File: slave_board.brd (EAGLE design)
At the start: 200 x 100 mm, 163 parts, among them IC3 ATMEGA2560-16AU, J1 OSTVN08A150, J11 1935161, J12 OSTVN06A150, J13 OSTVN08A150, J17 RJ45, J18 OSTVN08A150, J2 OSTVN08A150, J22 RJ45, J3 1935161, J4 OSTVN06A150, J6 1935161, J8 OSTVN08A150, K1 ORWH-SH-112D1F, Q1 PHB45NQ15T, Q2 PHB45NQ15T, Q3 BSS138L, Q5 BSS138L, Q7 PHB45NQ15T, Q8 IRFR9024TRPBF, U1 VNQ5E160KTR-E, U2 PCA9615, U3 INA213AIDCKT, U4 VNH7070ASTR, U5 VNH7070ASTR, U6 VNQ5E160KTR-E, U7 INA213AIDCKT, U8 LM340MP-5.0/NOPB, U9 LM340MP-5.0/NOPB, Y1 ABLS-16.000MHZ-B4-T

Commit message: Morning changes from board review
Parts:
- removed J12: OSTVN06A150, smoothio:6PIN_SCREW_TERMINAL
- added J16: OSTVN08A150, smoothio:8PIN_SCREW_TERMINAL
- added L1: 742792651, smoothio:742792651
- added R27, R28, R29, R30: 10k, SparkFun-Resistors:0603
- J1, J2: value OSTVN08A150 -> OSTVN06A150; device smoothio:8PIN_SCREW_TERMINAL -> smoothio:6PIN_SCREW_TERMINAL
- J5: value (none) -> OSTVN06A150; device SparkFun-Connectors:1X05 -> smoothio:6PIN_SCREW_TERMINAL
- moved J14 26.3 mm to (66.5, 29.1), turned to 0 degrees
- moved J5 14.5 mm to (84.7, 99.4), turned to 180 degrees
- moved J2 6.54 mm to (111.0, 99.4), turned to 180 degrees
- moved J1 6.50 mm to (139.9, 92.9)
- moved C18 1.59 mm to (96.4, 81.6)
- moved C30 1.59 mm to (103.0, 89.7)
- moved C15 1.59 mm to (96.7, 81.2)
- moved C31 1.59 mm to (92.9, 81.6)
- moved D6 1.59 mm to (100.5, 75.5)
- moved TP2 1.59 mm to (104.0, 72.3)
- moved JP19 1.59 mm to (96.7, 88.1)
- moved TP19 1.59 mm to (95.9, 90.7)
- moved U9 1.59 mm to (103.5, 83.1)
- moved J4 0.37 mm to (156.5, 93.0)
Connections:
- removed net CUP_SENSE0: IC3.72, J4.5
- removed net CUP_SENSE1: IC3.71, J12.5
- new net GND2: C19.-, C20.-, C21.-, D3.1, D3.3, D5.1, D5.3, L1.P$1, R1.1, R14.1, U3.5, U7.5
- new net LIMIT_SENSE: IC3.70, J1.1, R28.2
- net +5V: now also J1.3, J1.6, J16.5, J16.8, R27.1, R28.1, R29.1, R30.1; no longer J1.8, J12.3, J12.6, J2.5
- net A1: now also J5.3; no longer J5.2
- net A2: now also J5.2; no longer J5.1
- net B1: now also J5.4; no longer J5.3
- net B2: now also J5.5; no longer J5.4
- net CAROUSEL_POS: now also J1.4, R27.2; no longer J1.6
- net CUP_MASS1: now also J4.5; no longer J12.2
- net ELEV_ENC_A: now also J16.6, R29.2; no longer J2.8
- net ELEV_ENC_B: now also J16.3, R30.2; no longer J2.7
- net GND: now also J1.2, J16.1, J16.4, J16.7, L1.P$2; no longer C19.-, C20.-, C21.-, D3.1, D3.3, D5.1, D5.3, J1.1, J1.3, J1.7, J12.1, J12.4, R1.1, R14.1, U3.5, U7.5
- net THERMISTOR0: now also J2.5; no longer J1.2
- net THERMISTOR1: now also J16.2; no longer J1.4
- net V-STEPPER: now also J5.6; no longer J5.5
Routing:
- net GND: track 438.9 -> 341.9 mm, vias 62 -> 60
- net CUP_SENSE1: track 59.8 -> 0.00 mm, vias 1 -> 0
- net GND2: track 0.00 -> 54.9 mm, vias 0 -> 2
- net CUP_SENSE0: track 42.9 -> 0.00 mm, vias 1 -> 0
- net BLENDER0_EN: track 130.9 -> 104.1 mm, vias 3 -> 2
- net PIVOT_ENC_A: track 31.1 -> 4.73 mm
- net STEP: track 59.2 -> 33.0 mm
- net DIR: track 57.3 -> 32.6 mm
- net V-STEPPER: track 30.6 -> 8.13 mm
- net CAROUSEL_POS: track 40.9 -> 21.4 mm
- net THERMISTOR1: track 40.0 -> 21.0 mm
- net CUP_MASS1: track 62.7 -> 45.5 mm
- net CUP_MASS0: track 46.6 -> 31.0 mm
- net +5V: track 415.4 -> 401.0 mm
- net BLENDER1_EN: track 131.5 -> 117.7 mm, vias 4 -> 3
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
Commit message: Finished review changes
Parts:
- removed R27: 10k, SparkFun-Resistors:0603
- moved R28 187.8 mm to (156.4, 90.3), turned to 180 degrees
- moved R29 181.1 mm to (145.8, 90.6)
- moved R30 179.1 mm to (140.9, 90.6), turned to 180 degrees
- moved L1 99.9 mm to (55.9, 60.4), flipped to the bottom
- moved DRV8825 22.8 mm to (69.2, 75.1), turned to 0 degrees
- moved TP16 21.7 mm to (64.7, 96.2)
- moved R23 19.4 mm to (117.1, 90.7), turned to 180 degrees
- moved C34 19.4 mm to (117.1, 88.2), turned to 180 degrees
- moved J4 17.5 mm to (174.0, 93.0)
- moved C29 15.6 mm to (164.0, 87.6)
- moved R19 15.6 mm to (164.0, 90.2)
- moved J1 14.1 mm to (154.0, 93.0)
- moved TP6 12.1 mm to (123.6, 96.0)
- moved C10 10.3 mm to (132.5, 88.0), turned to 0 degrees
- moved R3 10.2 mm to (132.5, 90.5), turned to 0 degrees
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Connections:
- net +5V: no longer R27.1
- net CAROUSEL_POS: no longer R27.2
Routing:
- net V-STEPPER: track 8.13 -> 48.5 mm
- net +5V: track 401.0 -> 440.3 mm, vias 10 -> 11
- net LIMIT_SENSE: track 0.00 -> 38.9 mm
- net CAROUSEL_POS: track 21.4 -> 58.6 mm
- net CUP_MASS0: track 31.0 -> 65.0 mm
- net PIVOT_ENC_A: track 4.73 -> 33.7 mm
- net GND: track 341.9 -> 368.8 mm, vias 60 -> 42
- net CUP_MASS1: track 45.5 -> 72.4 mm
- net STEP: track 33.0 -> 56.3 mm
- net /EN: track 50.9 -> 74.2 mm, vias 2 -> 1
- net M0: track 46.6 -> 69.7 mm, vias 1 -> 2
- net DIR: track 32.6 -> 51.7 mm, vias 2 -> 0
- net M1: track 48.4 -> 67.5 mm, vias 1 -> 2
- net ELEV_ENC_B: track 44.4 -> 57.3 mm
- net M2: track 53.0 -> 65.7 mm, vias 1 -> 2
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- added copper zone on layer 1, net GND2
- added copper zone on layer 16, net GND2
- removed copper zone on layer 1, net GND

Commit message: Few more changes
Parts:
- added J12: (no value), SparkFun-Connectors:1X02
- moved J14 25.7 mm to (70.2, 3.63), turned to 180 degrees
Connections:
- net BLENDER0_EN: now also J12.1; no longer J14.1
- net BLENDER0_GATE: now also J14.1
- net BLENDER1_EN: now also J12.2; no longer J14.2
- net BLENDER1_GATE: now also J14.2
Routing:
- net BLENDER0_GATE: track 22.2 -> 44.2 mm, vias 0 -> 2
- net BLENDER1_GATE: track 22.5 -> 32.3 mm
- net CURR_SENS0: track 131.5 -> 132.5 mm
- net GND: track 368.8 -> 368.3 mm

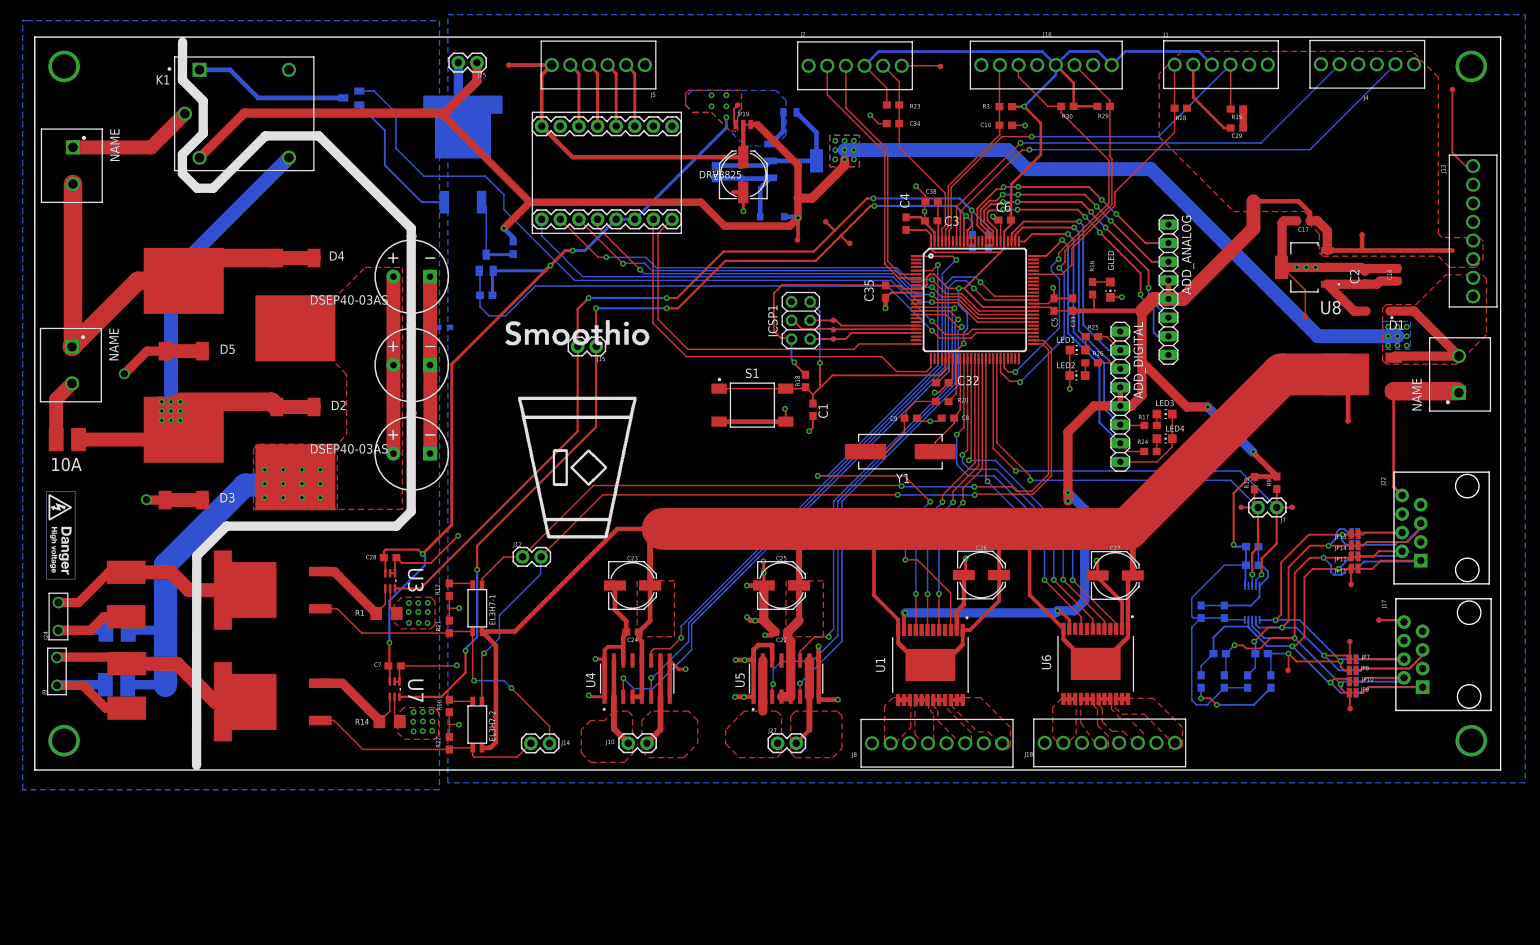
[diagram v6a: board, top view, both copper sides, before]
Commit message: Renumbered components
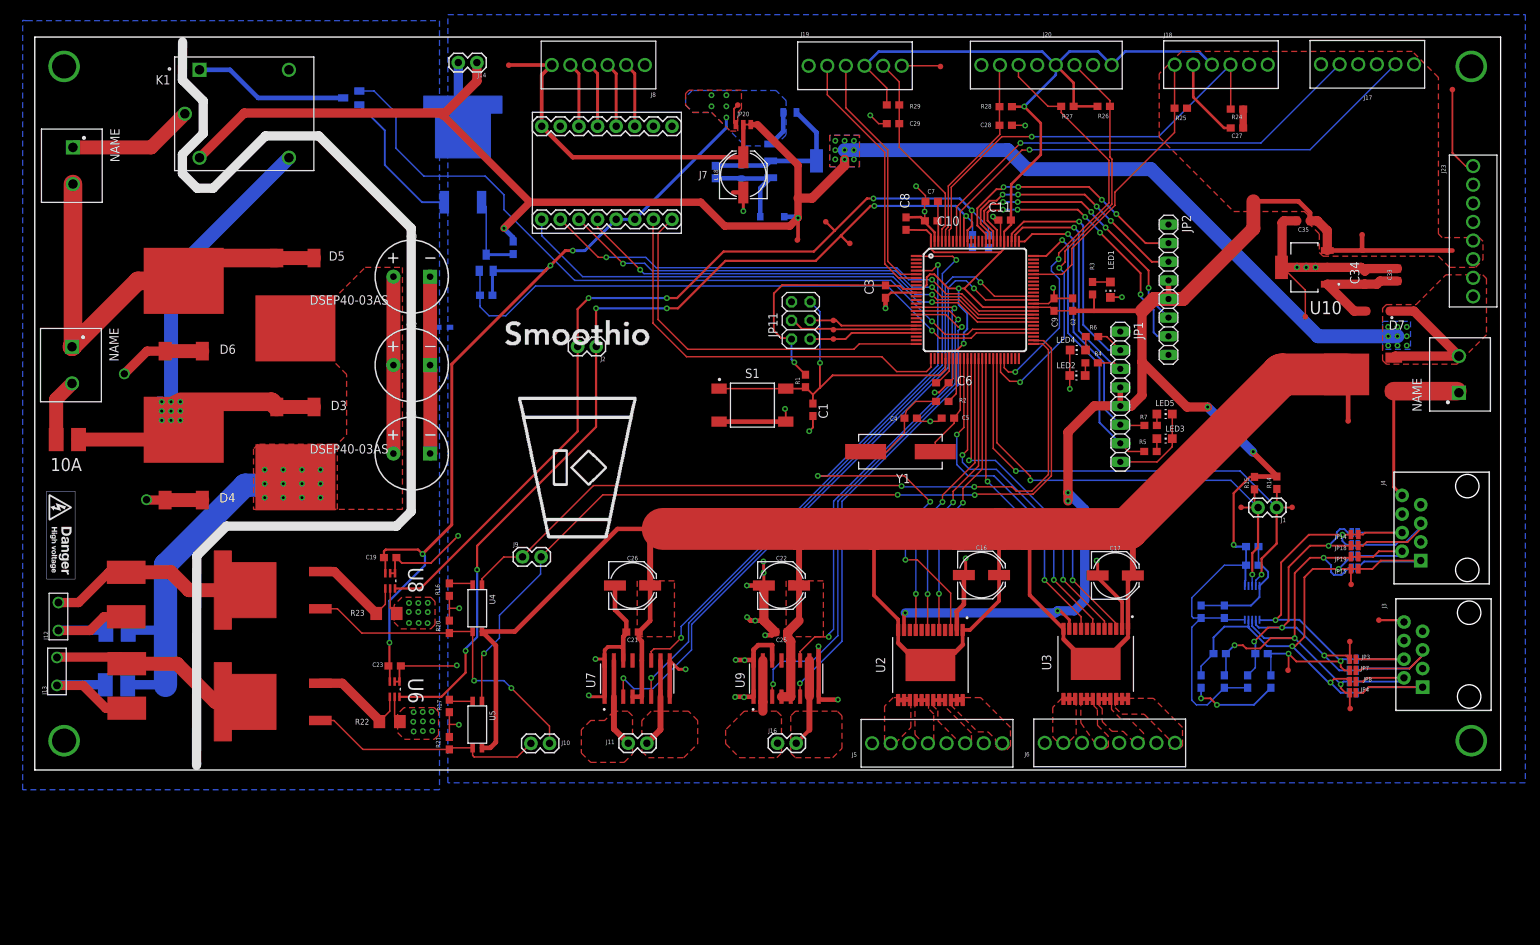
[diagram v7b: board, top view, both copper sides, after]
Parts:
- removed ADD_ANALOG: 8x1F-H8.5, SmartPrj:1X08
- removed DRV8825: DRV8825CARRIER, smoothio:DRV8825CARRIER
- removed EL3H7-1, EL3H7-2: EL3H7, smoothio:EL3H7
- removed GLED: GREEN, led:CHIP-LED0805
- removed ICSP1: 3x2M, SmartPrj:2X03
- removed J24: (no value), SparkFun-Connectors:1X02_BIG
- removed J25, J27: (no value), SparkFun-Connectors:1X02
- removed Q7: PHB45NQ15T, smoothio:PHB45NQ15T
- added J19: OSTVN06A150, smoothio:6PIN_SCREW_TERMINAL
- added J20, J23: OSTVN08A150, smoothio:8PIN_SCREW_TERMINAL
- added J21: 1935161, 1935161:PHOENIX_1935161
- added JP20: JUMPER-SMT_3_1-NC_TRACE_NO-SILK, SparkFun-Jumpers:SMT-JUMPER_3_1-NC_TRACE_NO-SILK
- added JP6: JUMPER-SMT_2_NO_NO-SILK, SparkFun-Jumpers:SMT-JUMPER_2_NO_NO-SILK
- added LED5: GREEN, led:CHIP-LED0805
- added Q4: PHB45NQ15T, smoothio:PHB45NQ15T
- added U10, U11: LM340MP-5.0/NOPB, LM340MP-5.0_NOPB:SOT230P700X180-4N
- C10: value 0.1uF -> 100n; device SparkFun-Capacitors:0603 -> rcl:C0603
- C11: value 0.1uF -> 100n
- C14: value 1.0uF -> 0.1uF
- C15: value 47uF -> 1.0uF; device SparkFun-Capacitors:PANASONIC_D -> rcl:C0603
- C16: value 1.0uF -> 47uF; device SparkFun-Capacitors:0603 -> SparkFun-Capacitors:PANASONIC_D
- C17: value 10uF -> 47uF; device SparkFun-Capacitors:0805 -> SparkFun-Capacitors:PANASONIC_D
- C18: value 100n -> 47uF; device SmartPrj:C0603-ROUND -> SparkFun-Capacitors:PANASONIC_D
- C19, C20, C21: value UCS2E470MHD1TO -> 0.1uF; device smoothio:UCS2E470MHD1TO -> rcl:C0603
- C2: value 100n -> 4.7uF; device SmartPrj:C0603-ROUND -> rcl:C0603
- C22: value 0.1uF -> 47uF; device rcl:C0603 -> SparkFun-Capacitors:PANASONIC_D
- C23, C25: value 47uF -> 0.1uF; device SparkFun-Capacitors:PANASONIC_D -> rcl:C0603
- C27: value 47uF -> 0.1uF; device SparkFun-Capacitors:PANASONIC_D -> SparkFun-Capacitors:0603
- C28: device rcl:C0603 -> SparkFun-Capacitors:0603
- C30: value 10uF -> UCS2E470MHD1TO; device SparkFun-Capacitors:0805 -> smoothio:UCS2E470MHD1TO
- C31: value 1.0uF -> UCS2E470MHD1TO; device SparkFun-Capacitors:0603 -> smoothio:UCS2E470MHD1TO
- C32: value 100n -> UCS2E470MHD1TO; device rcl:C0603 -> smoothio:UCS2E470MHD1TO
- C33: value 4.7uF -> 1.0uF; device rcl:C0603 -> SparkFun-Capacitors:0603
- C34: value 0.1uF -> 100n; device SparkFun-Capacitors:0603 -> SmartPrj:C0603-ROUND
- C35: value 100n -> 10uF; device rcl:C0603 -> SparkFun-Capacitors:0805
- C36, C7: value 0.1uF -> 1.0uF; device rcl:C0603 -> SparkFun-Capacitors:0603
- C37: value 0.1uF -> 100n; device rcl:C0603 -> SmartPrj:C0603-ROUND
- C38: value 1.0uF -> 10uF; device SparkFun-Capacitors:0603 -> SparkFun-Capacitors:0805
- C4: value 100n -> 15pF
- C5: value 100nF -> 15pF
- C8: value 15pF -> 100n
- C9: value 15pF -> 100nF
- D1: value MBR0530 -> SK520TR; device smoothio:MBR0530 -> smoothio:SK520TR
- D2: value DSEP40-03AS -> SK520TR; device smoothio:DSEP40-03AS -> smoothio:SK520TR
- D6: value MBR0530 -> DSEP40-03AS; device smoothio:MBR0530 -> smoothio:DSEP40-03AS
- D7, D8: value SK520TR -> MBR0530; device smoothio:SK520TR -> smoothio:MBR0530
- F1: value SSQ10 -> SSQ7; device smoothio:SSQ10 -> smoothio:SSQ7
- F3: value SSQ7 -> SSQ10; device smoothio:SSQ7 -> smoothio:SSQ10
- J1, J2: value OSTVN06A150 -> (none); device smoothio:6PIN_SCREW_TERMINAL -> SparkFun-Connectors:1X02
- J11: value 1935161 -> (none); device 1935161:PHOENIX_1935161 -> SparkFun-Connectors:1X02
- J12: device SparkFun-Connectors:1X02 -> SparkFun-Connectors:1X02_BIG
- J13: value OSTVN08A150 -> (none); device smoothio:8PIN_SCREW_TERMINAL -> SparkFun-Connectors:1X02_BIG
- J15: value (none) -> 1935161; device SparkFun-Connectors:1X02 -> 1935161:PHOENIX_1935161
- J16: value OSTVN08A150 -> (none); device smoothio:8PIN_SCREW_TERMINAL -> SparkFun-Connectors:1X02
- J17: value RJ45 -> OSTVN06A150; device SparkFun-Connectors:RJ45-8 -> smoothio:6PIN_SCREW_TERMINAL
- J18, J8: value OSTVN08A150 -> OSTVN06A150; device smoothio:8PIN_SCREW_TERMINAL -> smoothio:6PIN_SCREW_TERMINAL
- J22: value RJ45 -> 1935161; device SparkFun-Connectors:RJ45-8 -> 1935161:PHOENIX_1935161
- J3: value 1935161 -> RJ45; device 1935161:PHOENIX_1935161 -> SparkFun-Connectors:RJ45-8
- J4: value OSTVN06A150 -> RJ45; device smoothio:6PIN_SCREW_TERMINAL -> SparkFun-Connectors:RJ45-8
- J5: value OSTVN06A150 -> OSTVN08A150; device smoothio:6PIN_SCREW_TERMINAL -> smoothio:8PIN_SCREW_TERMINAL
- J6: value 1935161 -> OSTVN08A150; device 1935161:PHOENIX_1935161 -> smoothio:8PIN_SCREW_TERMINAL
- J7: value (none) -> DRV8825CARRIER; device SparkFun-Connectors:1X02 -> smoothio:DRV8825CARRIER
- J9: device SparkFun-Connectors:1X02_BIG -> SparkFun-Connectors:1X02
- JP11: value JUMPER-SMT_2_NC_TRACE_NO-SILK -> 3x2M; device SparkFun-Jumpers:SMT-JUMPER_2_NC_TRACE_NO-SILK -> SmartPrj:2X03
- JP15, JP16, JP17, JP18: value JUMPER-SMT_2_NO_NO-SILK -> JUMPER-SMT_2_NC_TRACE_NO-SILK; device SparkFun-Jumpers:SMT-JUMPER_2_NO_NO-SILK -> SparkFun-Jumpers:SMT-JUMPER_2_NC_TRACE_NO-SILK
- JP19: value JUMPER-SMT_3_1-NC_TRACE_NO-SILK -> JUMPER-SMT_2_NC_TRACE_NO-SILK; device SparkFun-Jumpers:SMT-JUMPER_3_1-NC_TRACE_NO-SILK -> SparkFun-Jumpers:SMT-JUMPER_2_NC_TRACE_NO-SILK
- JP2: value JUMPER-SMT_2_NC_TRACE_NO-SILK -> 8x1F-H8.5; device SparkFun-Jumpers:SMT-JUMPER_2_NC_TRACE_NO-SILK -> SmartPrj:1X08
- JP3, JP4, JP5: value JUMPER-SMT_2_NC_TRACE_NO-SILK -> JUMPER-SMT_2_NO_NO-SILK; device SparkFun-Jumpers:SMT-JUMPER_2_NC_TRACE_NO-SILK -> SparkFun-Jumpers:SMT-JUMPER_2_NO_NO-SILK
- Q1, Q2: value PHB45NQ15T -> BSS138L; device smoothio:PHB45NQ15T -> BSS138L:BSS138L
- Q3, Q5: value BSS138L -> PHB45NQ15T; device BSS138L:BSS138L -> smoothio:PHB45NQ15T
- R1: value CSR1206FT50L0 -> 10k; device smoothio:CSR1206FT50L0 -> SparkFun-Resistors:0603
- R10: value 220 -> 390
- R11: value 10k -> 390
- R12: value 220 -> 100
- R13: value 4.7k -> 390
- R14: value CSR1206FT50L0 -> 4.7k; device smoothio:CSR1206FT50L0 -> SparkFun-Resistors:0603
- R15: value 10k -> 4.7k
- R16, R17: value 1k -> 220
- R2: value 390 -> 0
- R20: value 0 -> 1M
- R22: value 1M -> CSR1206FT50L0; device SparkFun-Resistors:0603 -> smoothio:CSR1206FT50L0
- R23: value 51K -> CSR1206FT50L0; device SparkFun-Resistors:0603 -> smoothio:CSR1206FT50L0
- R24, R25, R26: value 1k -> 10k
- R28, R29: value 10k -> 51K
- R3: value 51K -> 1k
- R4, R7: value 100 -> 1k
- R5, R6: value 390 -> 1k
- R9: value 4.7k -> 100
- U1: value VNQ5E160KTR-E -> PCA9615; device VNQ5E160KTR-E:SOP80P1030X245-25N -> SparkFun_Differential_I2C_Breakout_PCA9615_Qwiic:SPARKFUN-IC-COMMS_TSSOP10
- U2: value PCA9615 -> VNQ5E160KTR-E; device SparkFun_Differential_I2C_Breakout_PCA9615_Qwiic:SPARKFUN-IC-COMMS_TSSOP10 -> VNQ5E160KTR-E:SOP80P1030X245-25N
- U3: value INA213AIDCKT -> VNQ5E160KTR-E; device INA213AIDCKT:SOT65P210X110-6N -> VNQ5E160KTR-E:SOP80P1030X245-25N
- U4, U5: value VNH7070ASTR -> EL3H7; device VNH7070ASTR:VNH7070ASTR -> smoothio:EL3H7
- U6: value VNQ5E160KTR-E -> INA213AIDCKT; device VNQ5E160KTR-E:SOP80P1030X245-25N -> INA213AIDCKT:SOT65P210X110-6N
- U7: value INA213AIDCKT -> VNH7070ASTR; device INA213AIDCKT:SOT65P210X110-6N -> VNH7070ASTR:VNH7070ASTR
- U8: value LM340MP-5.0/NOPB -> INA213AIDCKT; device LM340MP-5.0_NOPB:SOT230P700X180-4N -> INA213AIDCKT:SOT65P210X110-6N
- U9: value LM340MP-5.0/NOPB -> VNH7070ASTR; device LM340MP-5.0_NOPB:SOT230P700X180-4N -> VNH7070ASTR:VNH7070ASTR
- moved J13 203.3 mm to (3.03, 11.5), turned to 90 degrees
- moved D1 175.0 mm to (12.5, 23.8), turned to 270 degrees
- moved D7 175.0 mm to (183.1, 62.6), turned to 180 degrees
- moved J6 142.2 mm to (136.3, 0.45), turned to 0 degrees
- moved U8 131.9 mm to (48.5, 25.8), turned to 270 degrees
- moved R14 125.4 mm to (169.5, 39.2), turned to 90 degrees
- moved R11 113.7 mm to (162.3, 12.1), turned to 270 degrees
- moved R10 112.1 mm to (168.7, 12.1), flipped to the bottom
- moved J11 109.3 mm to (81.0, 3.66), turned to 0 degrees
- moved D8 108.9 mm to (100.5, 75.5), flipped to the bottom, turned to 0 degrees
- moved J7 107.7 mm to (69.2, 75.1), turned to 0 degrees
- moved R15 106.1 mm to (166.4, 39.1), flipped to the top
- moved R12 105.5 mm to (161.7, 15.9), flipped to the bottom, turned to 180 degrees
- moved R17 103.1 mm to (56.6, 8.74), turned to 90 degrees
- moved J5 102.9 mm to (112.7, 0.40), turned to 0 degrees
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- renumbered ADD_DIGITAL to JP1, IC3 to IC1, Q8 to Q6, R30 to R27
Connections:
- net +12V: now also D7.1, D8.1, J14.1, J22.2, J23.7, J23.8, JP20.3, R19.2; no longer D1.1, D6.1, J13.7, J13.8, J25.1, J3.2, JP19.3, R15.2
- net +5V: now also C15.1, C2.1, C27.1, C3.1, C8.1, C9.1, J17.3, J17.6, J18.3, J18.6, J19.4, J20.5, J20.8, J23.5, J23.6, JP11.2, JP2.4, JP2.5, R1.2, R11.2, R14.2, R15.2, R24.1, R25.1, R26.1, R28.2, R29.2, R3.1, R8.2, U1.1, U1.10, U10.3, U2.11, U3.11; no longer ADD_ANALOG.4, ADD_ANALOG.5, C17.1, C29.1, C32.1, C33.1, C4.1, C5.1, ICSP1.2, J1.3, J1.6, J13.5, J13.6, J16.5, J16.8, J2.4, J4.3, J4.6, R13.2, R16.1, R18.2, R19.1, R2.2, R23.2, R28.1, R29.1, R3.2, R6.2, R9.2, U1.11, U2.1, U2.10, U6.11, U8.3
- net /EN: now also J7./EN; no longer DRV8825./EN
- net /FLT: now also J7./FLT; no longer DRV8825./FLT
- net A1: now also J7.A1, J8.3; no longer DRV8825.A1, J5.3
- net A2: now also J7.A2, J8.2; no longer DRV8825.A2, J5.2
- net ADD_A12: now also JP2.2; no longer ADD_ANALOG.2
- net ADD_A13: now also JP2.3; no longer ADD_ANALOG.3
- net ADD_A14: now also JP2.6; no longer ADD_ANALOG.6
- net ADD_A15: now also JP2.7; no longer ADD_ANALOG.7
- net ADD_D22: now also R6.1; no longer R25.1
- net ADD_D23: now also R4.1; no longer R26.1
- net ADD_D24: now also R7.1; no longer R17.1
- net ADD_D25: now also R5.1; no longer R24.1
- net AREF: now also C10.1, C7.1; no longer C3.1, C38.1
- net B1: now also J7.B1, J8.4; no longer DRV8825.B1, J5.4
- net B2: now also J7.B2, J8.5; no longer DRV8825.B2, J5.5
- net BLENDER0-: now also D1.1, J12.P$2, Q4.2; no longer D7.1, J24.P$2, Q1.2
- net BLENDER0_EN: now also J9.1, U4.1; no longer EL3H7-1.1, J12.1
- net BLENDER0_GATE: now also J10.1, Q4.1, R20.2, U4.3; no longer EL3H7-1.3, J14.1, Q1.1, R21.2
- net BLENDER1-: now also D2.1, J13.P$2, Q5.2; no longer D8.1, J9.P$2, Q2.2
- net BLENDER1_EN: now also J9.2, U5.1; no longer EL3H7-2.1, J12.2
- net BLENDER1_GATE: now also J10.2, Q5.1, R21.2, U5.3; no longer EL3H7-2.3, J14.2, Q2.1, R22.2
- net CAROUSEL_POS: now also J18.4, R24.2; no longer J1.4, R19.2
- net COOLANT-: now also J14.2, Q3.2; no longer J25.2, Q7.2
- net COOLANT_EN: now also Q2.S, R18.1; no longer Q3.S, R11.1
- net COOLANT_GATE: now also Q2.D, Q3.1, R19.1; no longer Q3.D, Q7.1, R15.1
- net CUP_MASS0: now also J17.2; no longer J4.2
- net CUP_MASS1: now also J17.5; no longer J4.5
- net CURRSENS0-: now also Q4.3, R23.2, U8.4; no longer Q1.3, R1.2, U3.4
- net CURRSENS1-: now also Q5.3, R22.2, U6.4; no longer Q2.3, R14.2, U7.4
- net CURR_SENS0: now also C20.1, J2.1, U6.6; no longer C36.1, J15.1, U7.6
- net CURR_SENS1: now also C24.1, J2.2, U8.6; no longer C37.1, J15.2, U3.6
- net DIR: now also J7.DIR; no longer DRV8825.DIR
- net DSCL+: now also J3.5, J4.5, JP16.1, JP18.1, JP18.2, JP3.1, JP7.2, JP9.2, R8.1, R9.2, U1.7; no longer J17.5, J22.5, JP14.1, JP14.2, JP15.1, JP5.2, JP7.1, JP8.2, R2.1, R4.2, U2.7
- net DSCL-: now also J3.4, J4.4, JP12.1, JP12.2, JP14.1, JP14.2, JP3.2, JP5.2, JP7.1, JP9.1, R10.2, R9.1, U1.6; no longer J17.4, J22.4, JP13.1, JP13.2, JP15.2, JP16.1, JP4.1, JP4.2, JP7.2, JP8.1, R4.1, R5.2, U2.6
- net DSDA+: now also J3.2, J4.2, JP17.2, JP19.1, JP19.2, JP4.1, JP6.1, JP8.2, R11.1, R12.2, U1.8; no longer J17.2, J22.2, JP12.1, JP12.2, JP18.2, JP3.1, JP3.2, JP9.1, R6.1, R7.2, U2.8
- net DSDA-: now also J3.1, J4.1, JP13.1, JP13.2, JP15.1, JP15.2, JP4.2, JP6.2, JP8.1, R12.1, R13.2, U1.9; no longer J17.1, J22.1, JP11.1, JP11.2, JP17.2, JP18.1, JP2.1, JP2.2, JP9.2, R7.1, R8.2, U2.9
- net ELEV_CS: now also U9.13; no longer U5.13
- net ELEV_ENC_A: now also J20.6, R26.2; no longer J16.6, R29.2
- net ELEV_ENC_B: now also J20.3; no longer J16.3
- net ELEV_INA: now also U9.3; no longer U5.3
- net ELEV_INB: now also U9.6; no longer U5.6
- net ELEV_OUT_A: now also J16.1, U9.15, U9.2; no longer J27.1, U5.15, U5.2
- net ELEV_OUT_B: now also J16.2, U9.10, U9.7; no longer J27.2, U5.10, U5.7
- net ELEV_PWM: now also U9.11; no longer U5.11
- net EN: now also U1.2; no longer U2.2
- net FROZEN1: now also J5.8, U2.22, U2.23, U2.24; no longer J8.8, U1.22, U1.23, U1.24
- net FROZEN1_EN: now also U2.3; no longer U1.3
- net FROZEN2: now also J5.6, U2.19, U2.20, U2.21; no longer J8.6, U1.19, U1.20, U1.21
- net FROZEN2_EN: now also U2.5; no longer U1.5
- net FROZEN3: now also J5.4, U2.16, U2.17, U2.18; no longer J8.4, U1.16, U1.17, U1.18
- net FROZEN3_EN: now also U2.7; no longer U1.7
- net FROZEN4: now also J5.2, U2.13, U2.14, U2.15; no longer J8.2, U1.13, U1.14, U1.15
- net FROZEN4_EN: now also U2.9; no longer U1.9
- net FUSE0-: now also D1.2, F1.2, J12.P$1; no longer D7.2, F2.2, J24.P$1
- net FUSE1-: now also D2.2, F2.2, J13.P$1; no longer D8.2, F3.2, J9.P$1
- net F_STAT1: now also U2.4; no longer U1.4
- net F_STAT2: now also U2.6; no longer U1.6
- net F_STAT3: now also U2.8; no longer U1.8
- net F_STAT4: now also U2.10; no longer U1.10
- net GND: now also C15.2, C16.-, C17.-, C18.-, C19.2, C20.2, C21.2, C22.-, C23.2, C25.2, C27.2, C4.1, C5.1, C8.2, C9.2, J17.1, J17.4, J18.2, J19.1, J19.6, J20.1, J20.4, J20.7, J22.1, J23.1, J23.2, J23.3, J23.4, J3.3, J3.6, J3.7, J3.8, J4.3, J4.6, J4.7, J4.8, J5.1, J5.3, J5.5, J5.7, J6.1, J6.3, J6.5, J6.7, J7.GND, J7.GND1, JP11.6, JP2.1, JP2.8, LED5.C, Q1.S, Q3.3, R13.1, R16.1, R17.1, R20.1, U1.5, U10.2, U10.4, U11.2, U11.4, U2.2, U6.1, U7.14, U7.16, U7.8, U7.9, U8.1, U9.1, U9.14, U9.16, U9.8, U9.9; no longer ADD_ANALOG.1, ADD_ANALOG.8, C15.-, C16.2, C17.2, C18.2, C22.2, C23.-, C25.-, C27.-, C30.2, C31.2, C32.2, C4.2, C5.2, C8.1, C9.1, DRV8825.GND, DRV8825.GND1, GLED.C, ICSP1.6, J1.2, J1.5, J13.1, J13.2, J13.3, J13.4, J16.1, J16.4, J16.7, J17.3, J17.6, J17.7, J17.8, J18.1, J18.3, J18.7, J2.1, J2.6, J22.3, J22.6, J22.7, J22.8, J3.1, J4.1, J4.4, J8.1, J8.3, J8.5, J8.7, Q5.S, Q7.3, R12.1, R22.1, R5.1, R8.1, U1.2, U2.5, U3.1, U4.1, U4.14, U4.16, U4.8, U4.9, U5.1, U5.14, U5.16, U5.8, U5.9, U7.2, U8.4, U9.2, U9.4
- net GND2: now also C30.-, C31.-, C32.-, D4.1, D4.3, D6.1, D6.3, R22.1, R23.1, U6.5, U8.5; no longer C19.-, C20.-, C21.-, D3.1, D3.3, D5.1, D5.3, R1.1, R14.1, U3.5, U7.5
- net HEATPUMP_EN: now also Q1.G; no longer Q5.G
- net LIMIT_SENSE: now also J18.1, R25.2; no longer J1.1, R28.2
- net LIQUID1: now also J6.8, U3.22, U3.23, U3.24; no longer J18.8, U6.22, U6.23, U6.24
- net LIQUID1_EN: now also U3.3; no longer U6.3
- net LIQUID2: now also J6.6, U3.19, U3.20, U3.21; no longer J18.6, U6.19, U6.20, U6.21
- net LIQUID2_EN: now also U3.5; no longer U6.5
- net LIQUID3: now also J6.4, U3.16, U3.17, U3.18; no longer J18.4, U6.16, U6.17, U6.18
- net LIQUID3_EN: now also U3.7; no longer U6.7
- net L_STAT1: now also U3.4; no longer U6.4
- net L_STAT2: now also U3.6; no longer U6.6
- net L_STAT3: now also U3.8; no longer U6.8
- net M+: now also D3.1, D3.3, D4.4, F3.2; no longer D2.1, D2.3, D3.4, F1.2
- net M+_IN: now also F3.1, J21.2; no longer F1.1, J6.2
- net M-: now also D5.1, D5.3, D6.4, J15.2, J21.1; no longer D4.1, D4.3, D5.4, J11.2, J6.1
- net M0: now also J7.M0; no longer DRV8825.M0
- net M1: now also J7.M1; no longer DRV8825.M1
- net M2: now also J7.M2; no longer DRV8825.M2
- net MISO: now also JP11.1; no longer ICSP1.1
- net MOSI: now also JP11.4; no longer ICSP1.4
- net N$1: now also C33.1, C34.1, D7.2, U10.1; no longer C16.1, C2.1, D1.2, U8.1
- net N$10: now also R4.2; no longer R26.2
- net N$13: now also C4.2, R2.1; no longer C9.2, R20.1
- net N$14: now also R16.2, U4.2; no longer EL3H7-1.2, R12.2
- net N$2: now also LED5.A, R7.2; no longer LED3.A, R17.2
- net N$3: now also LED1.A, R3.2; no longer GLED.A, R16.2
- net N$4: now also C36.1, C37.1, D8.2, U11.1; no longer C18.1, C31.1, D6.2, U9.1
- net N$5: now also LED3.A, R5.2; no longer LED4.A, R24.2
- net N$7: now also R17.2, U5.2; no longer EL3H7-2.2, R10.2
- net N$9: now also LED4.A, R6.2; no longer LED1.A, R25.2
- net PIVOT_CS: now also U7.13; no longer U4.13
- net PIVOT_ENC_A: now also J19.3; no longer J2.3
- net PIVOT_ENC_B: now also J19.2; no longer J2.2
- net PIVOT_INA: now also U7.3; no longer U4.3
- net PIVOT_INB: now also U7.6; no longer U4.6
- net PIVOT_OUT_A: now also J11.1, U7.15, U7.2; no longer J10.1, U4.15, U4.2
- net PIVOT_OUT_B: now also J11.2, U7.10, U7.7; no longer J10.2, U4.10, U4.7
- net PIVOT_PWM: now also U7.11; no longer U4.11
- net POWDER1: now also J6.2, U3.13, U3.14, U3.15; no longer J18.2, U6.13, U6.14, U6.15
- net POWDER1_EN: now also U3.9; no longer U6.9
- net P_STAT1: now also U3.10; no longer U6.10
- net RELAY-: now also Q1.D; no longer Q5.D
- net RESET: now also JP11.5, R1.1; no longer ICSP1.5, R18.1
- net SCK: now also JP11.3; no longer ICSP1.3
- net SCL: now also J1.1, R14.1, U1.4; no longer J7.1, R9.1, U2.4
- net SDA: now also J1.2, R15.1, U1.3; no longer J7.2, R13.1, U2.3
- net STEP: now also J7.STEP; no longer DRV8825.STEP
- net THERMISTOR0: now also C29.1, J19.5, R29.1; no longer C34.1, J2.5, R23.1
- net THERMISTOR1: now also C28.1, J20.2, R28.1; no longer C10.1, J16.2, R3.1
- net V-12V_PROT: now also C16.+, C17.+, C21.1, C22.+, C25.1, U2.1, U2.12, U2.25, U3.1, U3.12, U3.25, U7.12, U7.4, U7.5, U9.12, U9.4, U9.5; no longer C22.1, C23.+, C24.1, C25.+, C27.+, EL3H7-1.4, EL3H7-2.4, U1.1, U1.12, U1.25, U4.12, U4.5, U5.12, U5.5, U6.1, U6.12, U6.25
- net V-5_LOAD: now also C19.1, C23.1, C38.1, J7./RESET, J7./SLEEP, JP20.1, Q2.G, R18.2, U11.3, U6.3, U8.3; no longer C28.1, C30.1, C7.1, DRV8825./RESET, DRV8825./SLEEP, JP19.1, Q3.G, R11.2, U3.3, U7.3, U9.3
- net V-HEATPUMP: now also J15.1; no longer J11.1
- net V-HVDC: now also C30.+, C31.+, C32.+, D3.4, D5.4, F1.1; no longer C19.+, C20.+, C21.+, D2.4, D4.4, F3.1
- net V-STEPPER: now also C18.+, J7.V-STEPPER, J8.6, JP20.2; no longer C15.+, DRV8825.V-STEPPER, J5.6, JP19.2
- net XTAL1: now also C5.2; no longer C8.2
- net XTAL2: now also R2.2; no longer R20.2

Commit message: Added labels to connectors
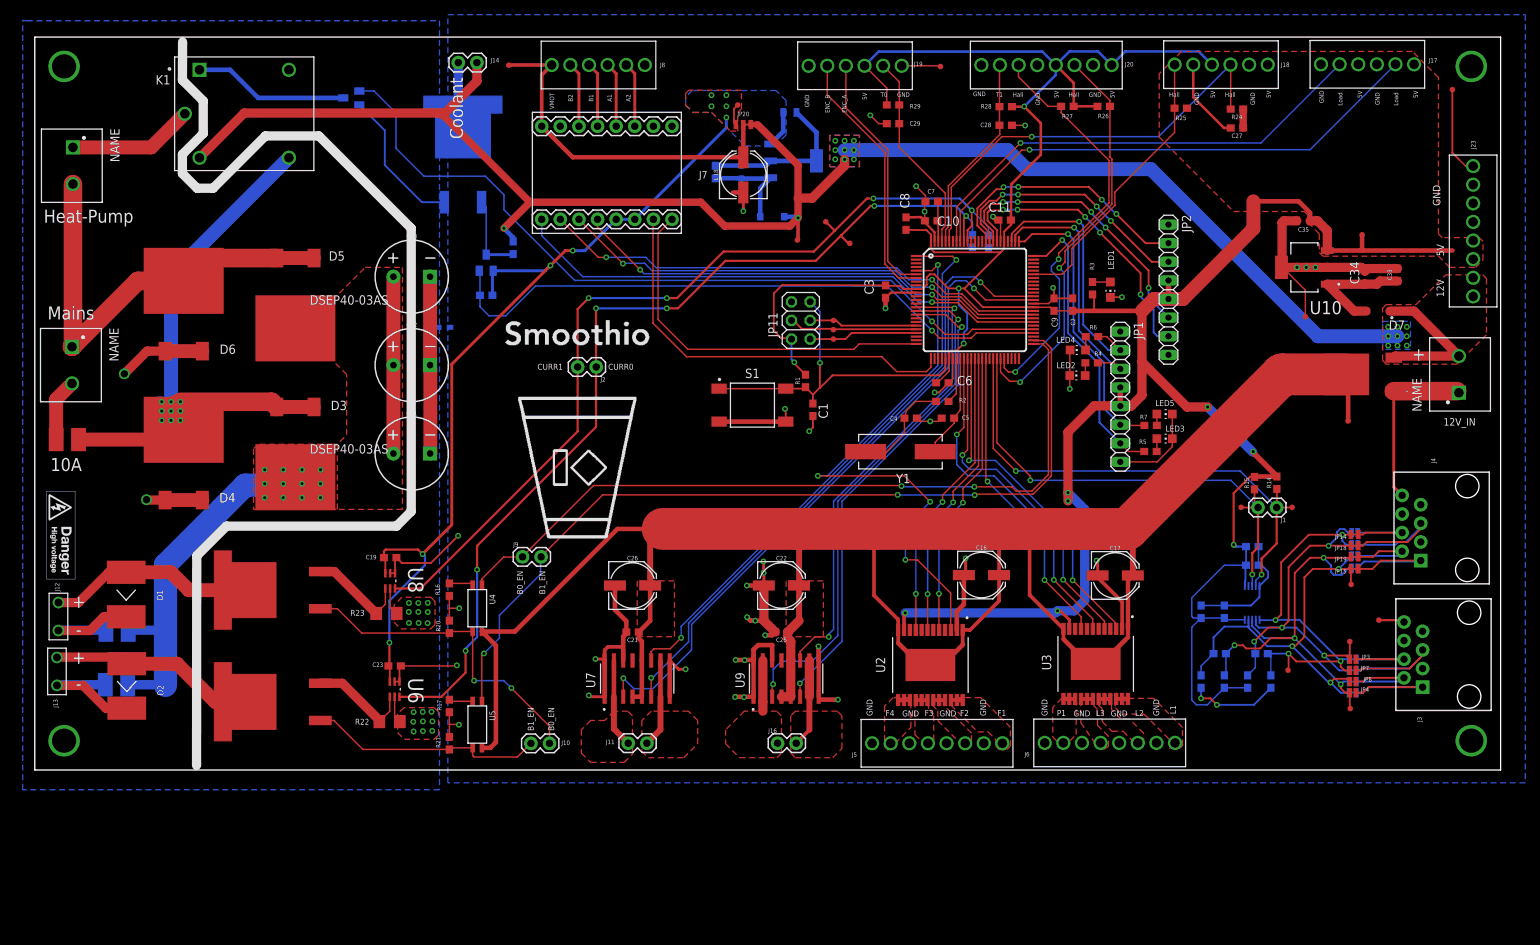
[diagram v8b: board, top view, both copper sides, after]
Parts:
- moved J2 2.79 mm to (76.6, 55.0)
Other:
- board text added: "+"
- board text added: "-"
- board text added: "12V"
- board text added: "12V_IN"
- board text added: "5V"
- board text added: "A1"
- board text added: "A2"
- board text added: "B0_EN"
- board text added: "B1"
- board text added: "B1_EN"
- board text added: "B2"
- board text added: "CURR0"
- board text added: "CURR1"
- board text added: "Coolant"
- board text added: "ENC_A"
- board text added: "ENC_B"
- board text added: "F1"
- board text added: "F2"
- board text added: "F3"
- board text added: "F4"
- board text added: "GND"
- board text added: "Hall"
- board text added: "Heat-Pump"
- board text added: "L1"
- board text added: "L2"
- board text added: "L3"
- board text added: "Load"
- board text added: "Mains"
- board text added: "P1"
- board text added: "T0"
- board text added: "T1"
- board text added: "VMOT"
